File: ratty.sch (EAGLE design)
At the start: 95 parts, among them IC2 L293DD, Q1 BS170, Q2 BS170, Q3 BS170, Q5 BS170, U1 ITG-32001:1

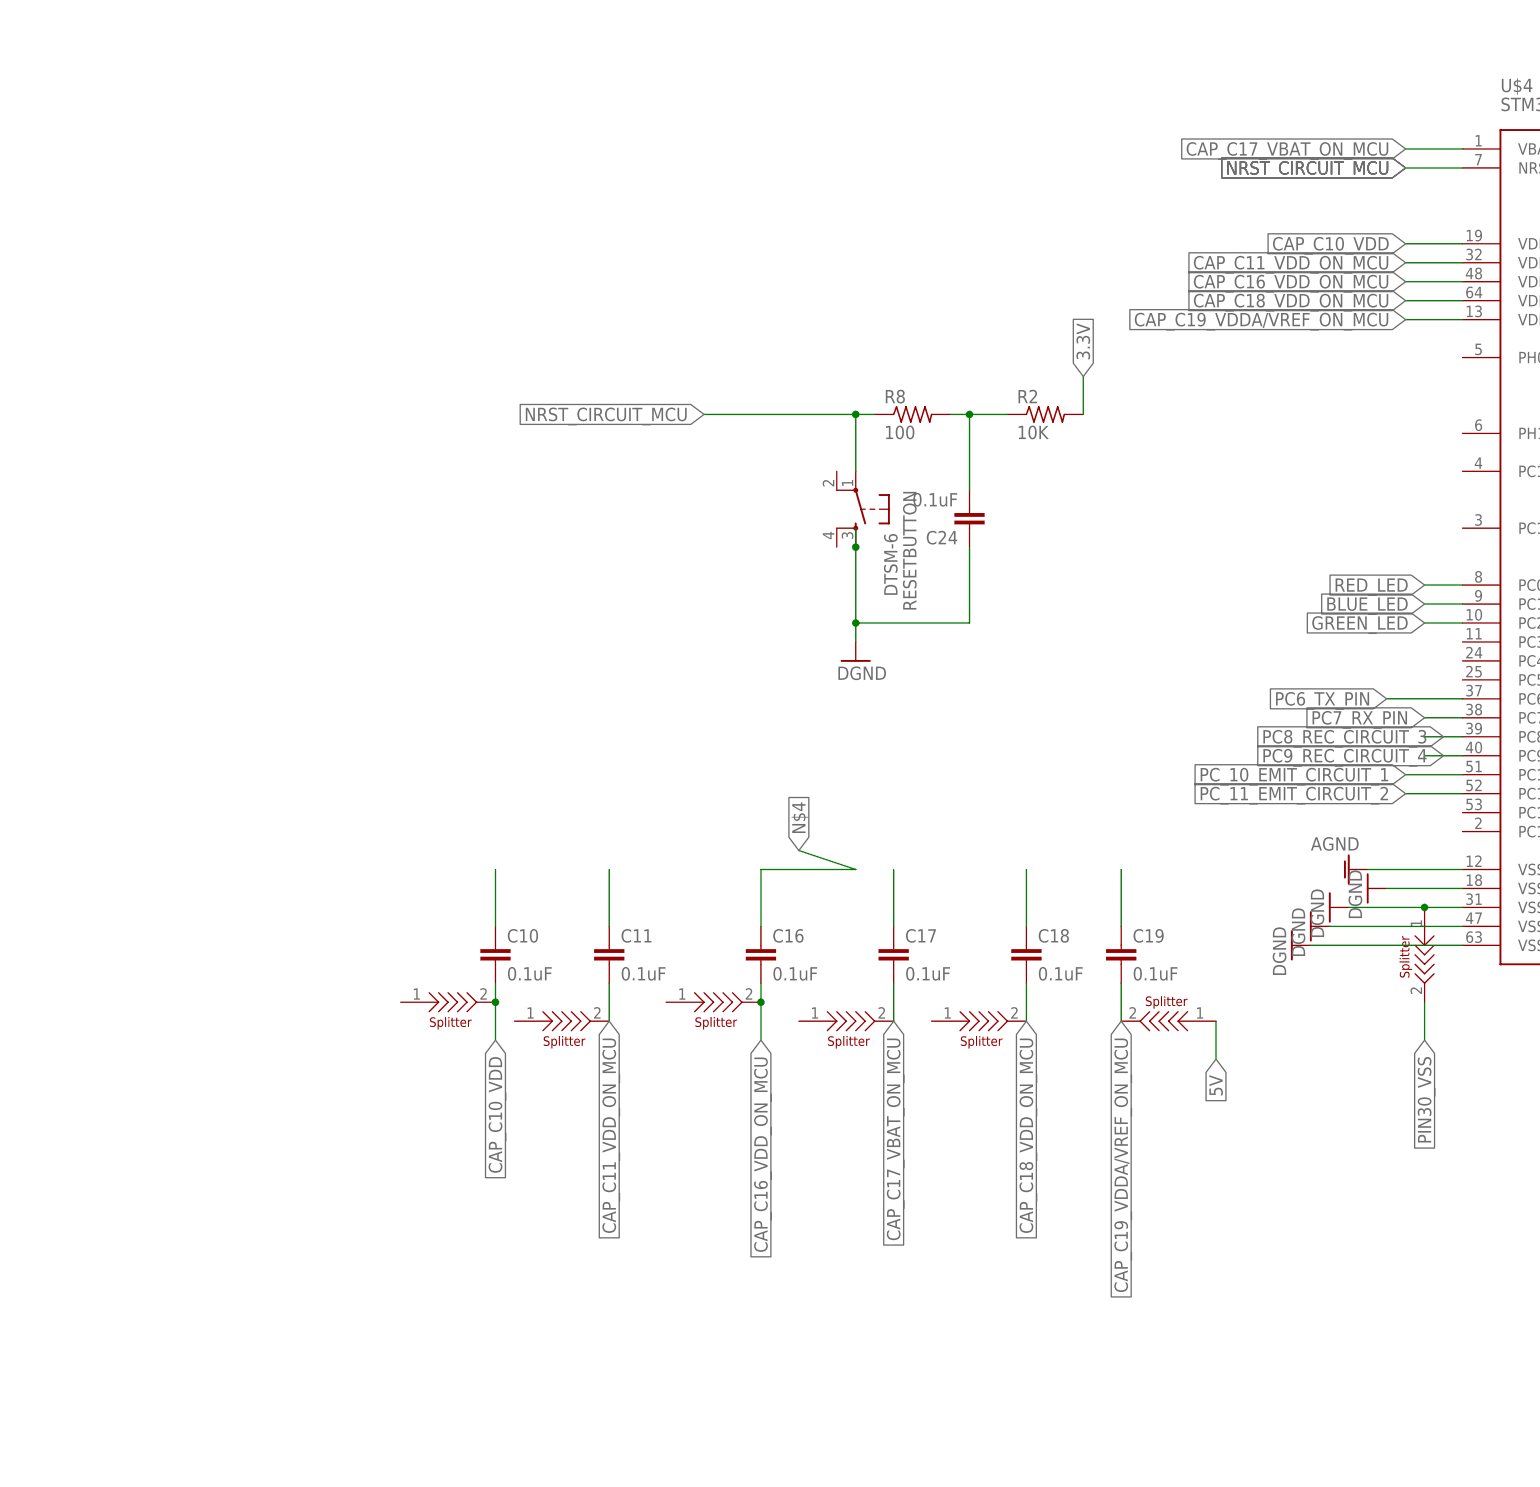
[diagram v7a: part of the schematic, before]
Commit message: Fixed the VDD and VSS of the MCU
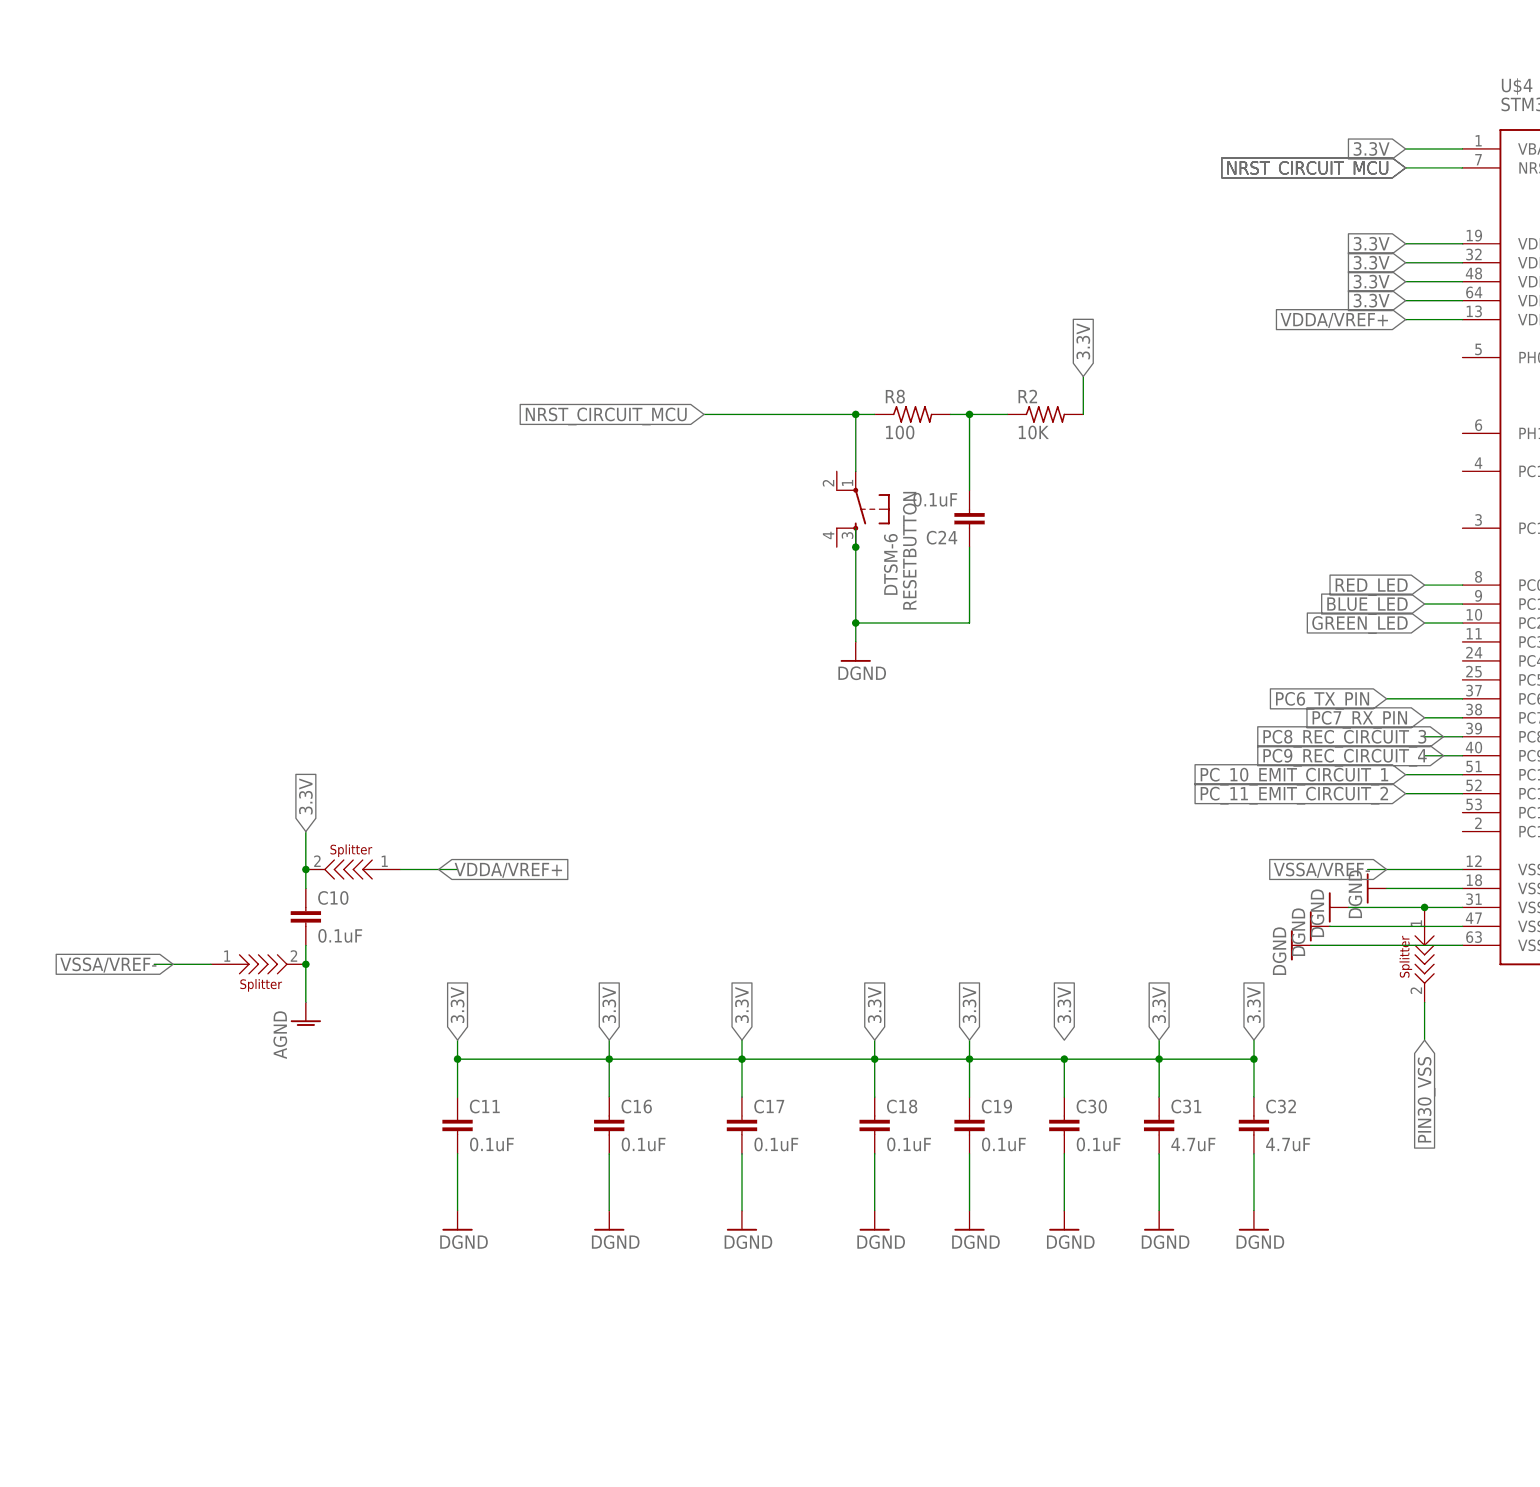
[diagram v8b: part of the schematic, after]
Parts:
- removed U$10, U$12, U$14, U$20, U$21: SPLITTER, splitter:SPLITTER
- added C30: 0.1uF, rcl:C-EUC0603
- added C31, C32: 4.7uF, rcl:C-EUC0603
- added U$22: SPLITTER, splitter:SPLITTER
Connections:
- removed net CAP_C10_VDD: C10.2, U$7.2
- removed net CAP_C11_VDD_ON_MCU: C11.2, U$10.2
- removed net CAP_C16_VDD_ON_MCU: C16.2, U$12.2
- removed net CAP_C17_VBAT_ON_MCU: C17.2, U$14.2, U$4.VBAT
- removed net CAP_C18_VDD_ON_MCU: C18.2, U$20.2
- removed net CAP_C19_VDDA/VREF_ON_MCU: C19.2, U$21.2
- removed net N$1: C10.1
- removed net N$3: C11.1
- removed net N$4: C16.1
- removed net N$5: C17.1
- removed net N$6: C18.1
- new net VDDA/VREF+: U$22.1
- new net VSSA/VREF-: U$7.1
- net 3.3V: now also C10.1, C11.1, C16.1, C17.1, C18.1, C19.1, C30.1, C31.1, C32.1, U$22.2, U$4.VBAT
- net 5V: no longer U$21.1
- net AGND: now also C10.2, U$7.2
- net DGND: now also C11.2, C16.2, C17.2, C18.2, C19.2, C30.2, C31.2, C32.2; no longer C19.1
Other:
- moved on the sheet: C10, C11, C16, C17, C18, C19
